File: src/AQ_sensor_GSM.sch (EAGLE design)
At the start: 82 parts, among them IC1 MIC29302WU, IC2 MCP73831/OT, J1 F-1X03-SIP-100-32, J2 SIM8060-6-1-14-00-A, Q1 MMBT2222, Q2 MMBT2222, Q3 MMBT2222, U2 TEXAS_INSTRUMENTS_SN74HC125TE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, U3 TEXAS_INSTRUMENTS_LM1117IMP-3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, U4 EC200UCNAB-N05-SNNSA, X1 53048-08

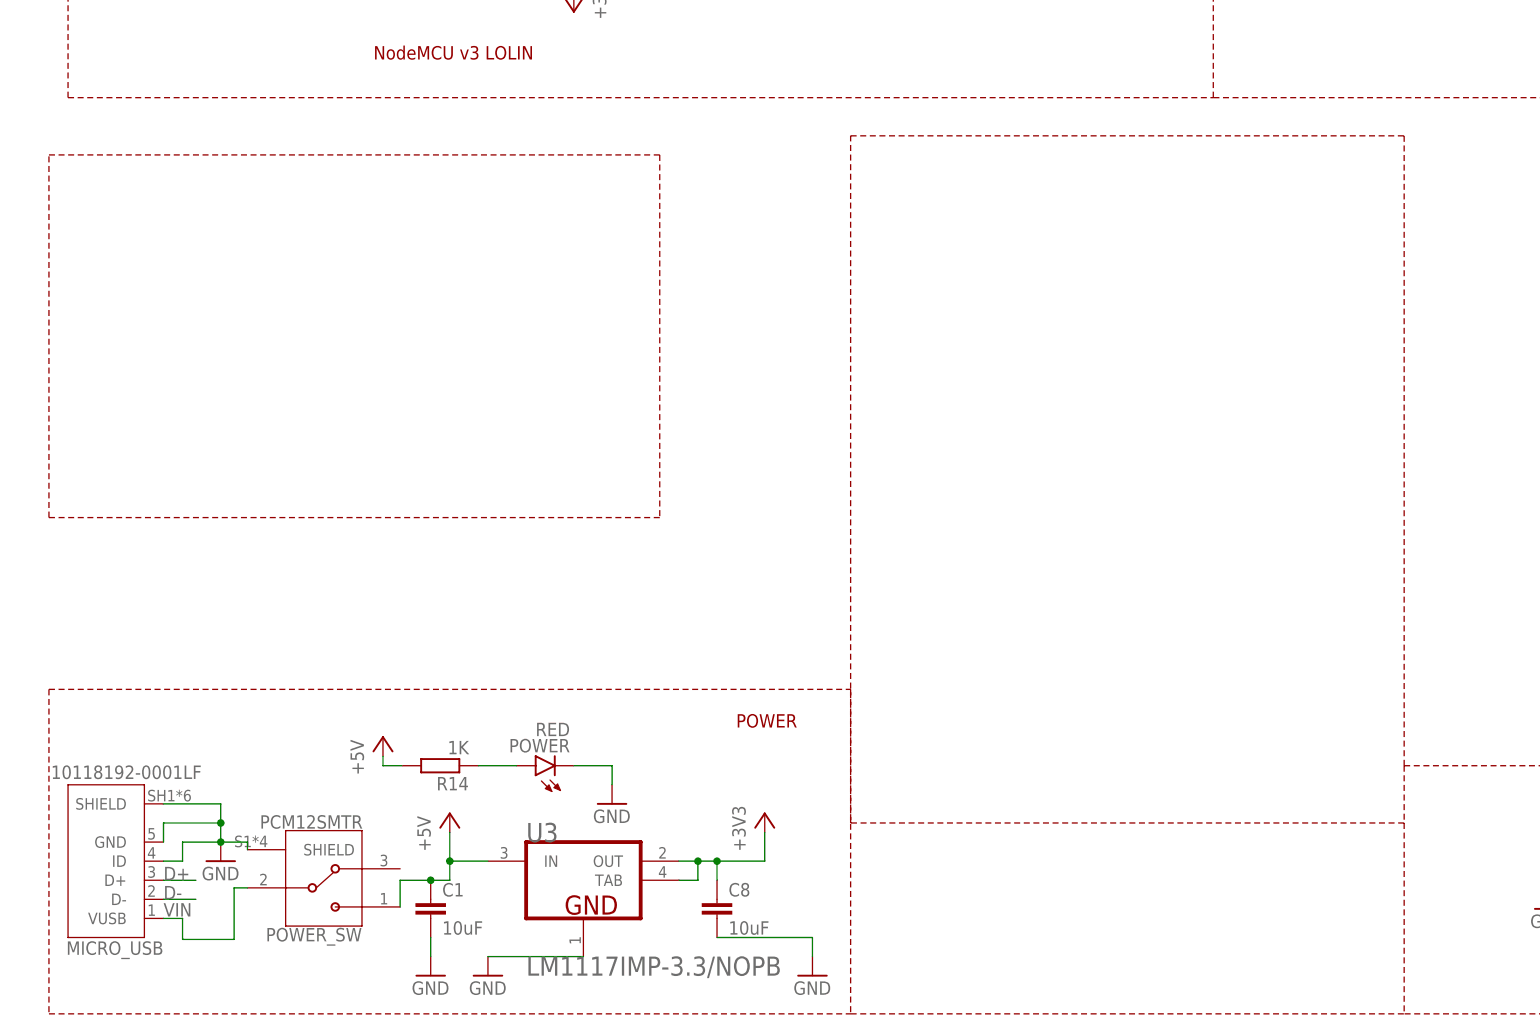
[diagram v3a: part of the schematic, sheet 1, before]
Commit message: Updated GSM antenna positions, pms connector, USB, and battery connector positions
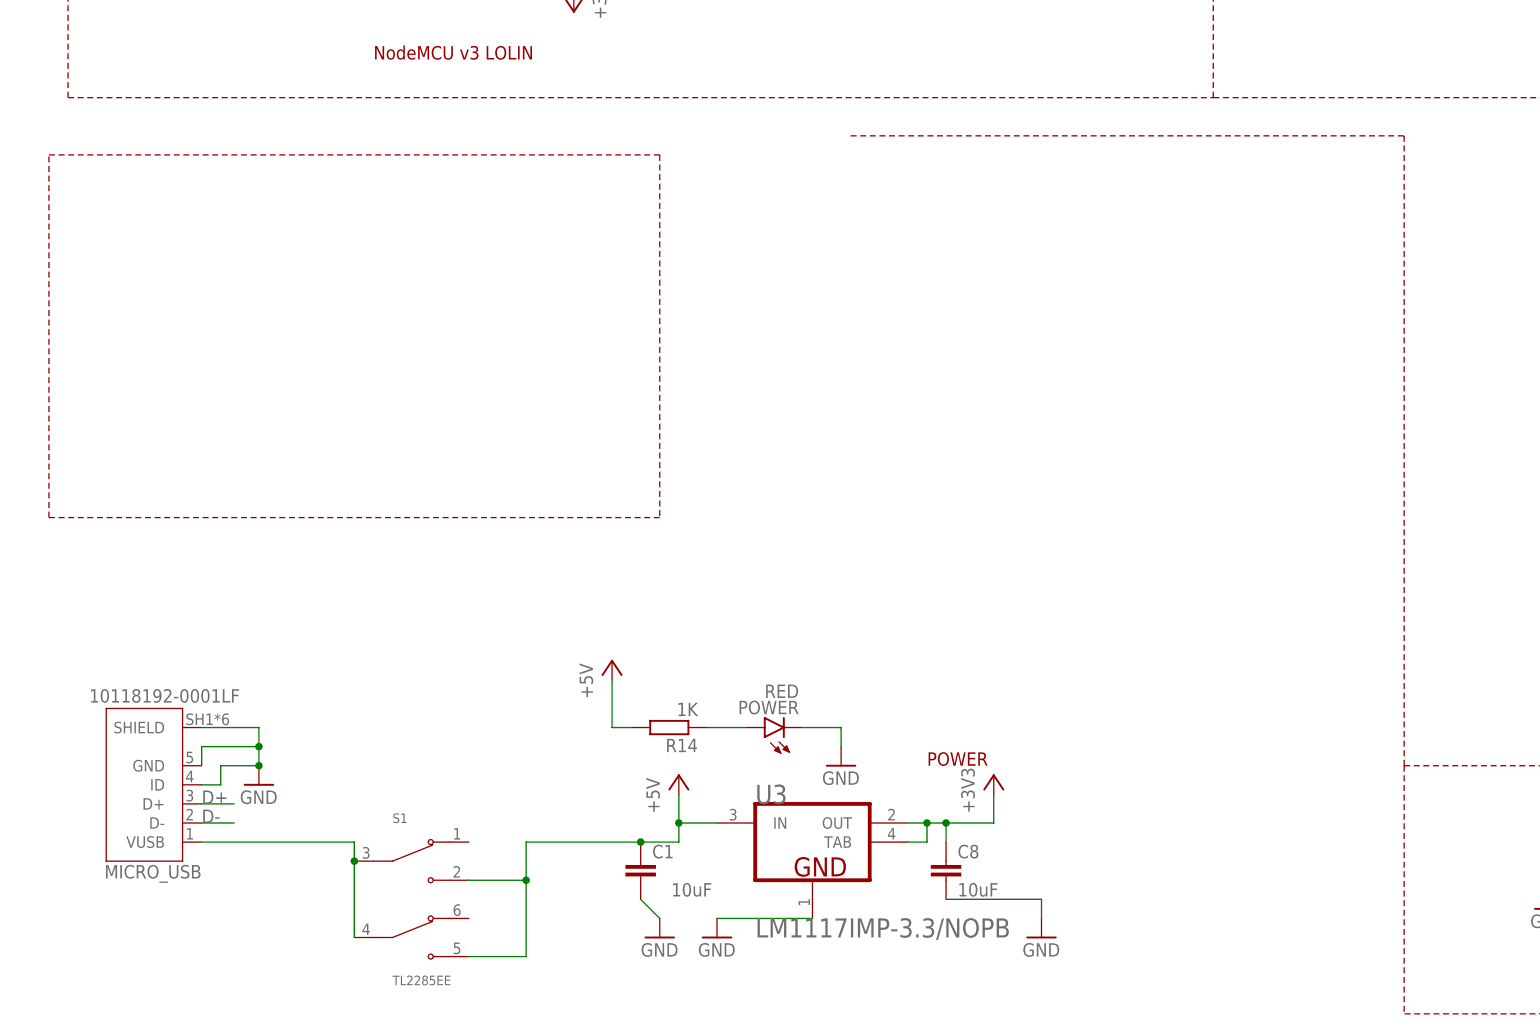
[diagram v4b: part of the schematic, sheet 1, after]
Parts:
- removed POWER_SW: PCM12SMTR, AQ_sensor_GSM:PCM12SMTR
- added S1: TL2285EE, TL2285EE:TL2285EE
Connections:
- removed net VIN: MICRO_USB.VUSB, POWER_SW.2
- new net N$17: MICRO_USB.VUSB, S1.COM1, S1.COM2
- net +5V: now also S1.NO1, S1.NO2; no longer POWER_SW.1
- net GND: no longer POWER_SW.SHIELD
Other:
- moved on the sheet: C1, C8, MICRO_USB, POWER, R14, U3

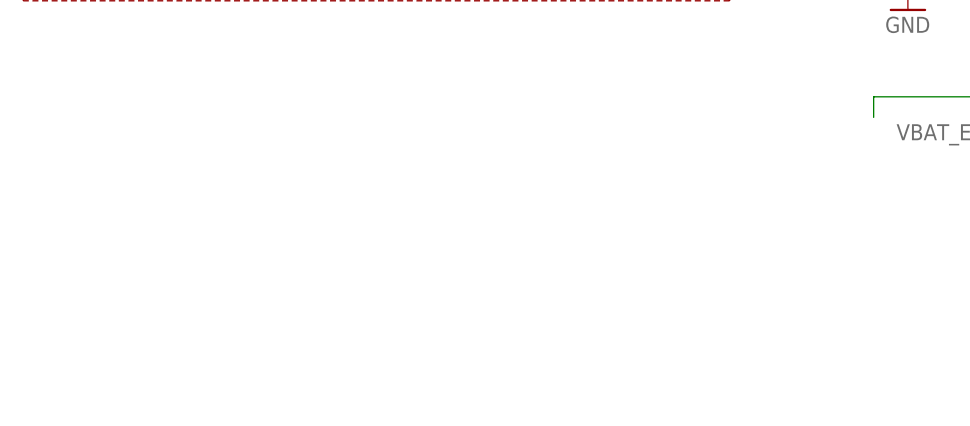
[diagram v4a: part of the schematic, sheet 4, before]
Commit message: Added dC jack
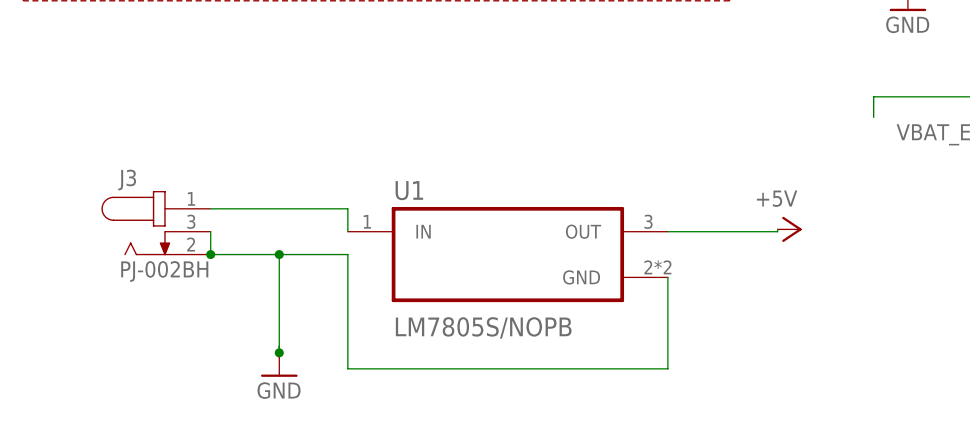
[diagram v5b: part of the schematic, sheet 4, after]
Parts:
- added J3: PJ-002BH, PJ-002BH:PJ-002BH
- added U1: LM7805S/NOPB, LM7805S_NOPB:LM7805S/NOPB
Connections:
- new net N$24: J3.1, U1.IN
- net +5V: now also U1.OUT
- net GND: now also J3.2, J3.3, U1.GND
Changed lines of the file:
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@@
 <part name="BT_ANT" library="SparkFun-Connectors" library_urn="urn:adsk.eagle:library:513" deviceset="CONN_01" device="" package3d_urn="urn:adsk.eagle:package:38028/1"/>
 <part name="S1" library="TL2285EE" deviceset="TL2285EE" device="" override_package3d_urn="urn:adsk.eagle:package:43003845/2" override_package_urn="urn:adsk.eagle:footprint:43003846/1"/>
+<part name="J3" library="PJ-002BH" deviceset="PJ-002BH" device="" override_package3d_urn="urn:adsk.eagle:package:43007122/2" override_package_urn="urn:adsk.eagle:footprint:43007123/1"/>
+<part name="U1" library="LM7805S_NOPB" deviceset="LM7805S/NOPB" device="" override_package3d_urn="urn:adsk.eagle:package:43007127/2" override_package_urn="urn:adsk.eagle:footprint:43007128/1"/>
+<part name="GND13" library="supply1" library_urn="urn:adsk.eagle:library:371" deviceset="GND" device=""/>
+<part name="P+10" library="supply1" library_urn="urn:adsk.eagle:library:371" deviceset="+5V" device=""/>
 </parts>
 <sheets>
@@
 <attribute name="VALUE" x="57.15" y="230.378" size="1.778" layer="96"/>
 </instance>
+<instance part="J3" gate="G$1" x="-88.9" y="144.78" smashed="yes">
+<attribute name="NAME" x="-93.98" y="149.86" size="1.778" layer="95"/>
+<attribute name="VALUE" x="-93.98" y="139.7" size="1.778" layer="96"/>
+</instance>
+<instance part="U1" gate="G$1" x="-50.8" y="142.24" smashed="yes">
+<attribute name="NAME" x="-63.5" y="148.32" size="2.0828" layer="95" ratio="10" rot="SR0"/>
+<attribute name="VALUE" x="-63.5" y="133.16" size="2.0828" layer="96" ratio="10" rot="SR0"/>
+</instance>
+<instance part="GND13" gate="1" x="-76.2" y="128.778" smashed="yes">
+<attribute name="VALUE" x="-78.74" y="126.238" size="1.778" layer="96"/>
+</instance>
+<instance part="P+10" gate="1" x="-18.288" y="145.034" smashed="yes" rot="R270">
+<attribute name="VALUE" x="-23.368" y="147.574" size="1.778" layer="96"/>
+</instance>
 </instances>
 <busses>
@@
 <wire x1="59.69" y1="235.458" x2="59.69" y2="246.38" width="0.1524" layer="91"/>
 <wire x1="59.69" y1="246.38" x2="60.96" y2="246.38" width="0.1524" layer="91"/>
+</segment>
+<segment>
+<pinref part="GND13" gate="1" pin="GND"/>
+<wire x1="-76.2" y1="132.08" x2="-76.2" y2="131.318" width="0.1524" layer="91"/>
+<pinref part="J3" gate="G$1" pin="3"/>
+<pinref part="J3" gate="G$1" pin="2"/>
+<wire x1="-83.82" y1="144.78" x2="-83.82" y2="142.24" width="0.1524" layer="91"/>
+<wire x1="-83.82" y1="142.24" x2="-76.2" y2="142.24" width="0.1524" layer="91"/>
+<wire x1="-76.2" y1="142.24" x2="-68.58" y2="142.24" width="0.1524" layer="91"/>
+<wire x1="-68.58" y1="142.24" x2="-68.58" y2="129.54" width="0.1524" layer="91"/>
+<junction x="-83.82" y="142.24"/>
+<pinref part="U1" gate="G$1" pin="GND"/>
+<wire x1="-68.58" y1="129.54" x2="-33.02" y2="129.54" width="0.1524" layer="91"/>
+<wire x1="-33.02" y1="129.54" x2="-33.02" y2="139.7" width="0.1524" layer="91"/>
+<wire x1="-76.2" y1="131.318" x2="-76.2" y2="142.24" width="0.1524" layer="91"/>
+<junction x="-76.2" y="131.318"/>
+<junction x="-76.2" y="142.24"/>
 </segment>
 </net>
@@
 <wire x1="-7.62" y1="187.96" x2="-7.62" y2="205.74" width="0.1524" layer="91"/>
 <wire x1="-7.62" y1="205.74" x2="58.42" y2="205.74" width="0.1524" layer="91"/>
+</segment>
+<segment>
+<pinref part="P+10" gate="1" pin="+5V"/>
+<pinref part="U1" gate="G$1" pin="OUT"/>
+<wire x1="-20.828" y1="145.034" x2="-20.828" y2="144.78" width="0.1524" layer="91"/>
+<wire x1="-20.828" y1="144.78" x2="-33.02" y2="144.78" width="0.1524" layer="91"/>
 </segment>
 </net>
@@
 </segment>
 </net>
+<net name="N$24" class="0">
+<segment>
+<pinref part="J3" gate="G$1" pin="1"/>
+<pinref part="U1" gate="G$1" pin="IN"/>
+<wire x1="-83.82" y1="147.32" x2="-68.58" y2="147.32" width="0.1524" layer="91"/>
+<wire x1="-68.58" y1="147.32" x2="-68.58" y2="144.78" width="0.1524" layer="91"/>
+</segment>
+</net>

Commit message: Rearrange USB port and DC jack
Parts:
- removed C14: EEEFT1E101AV, 100uf 25v capacitor:EEEFT1E101AV
- removed C5: EEEFN1C471P, EEEFN1C471P:EEEFN1C471P
- removed D4: ON_SEMI_1N4148WSON_SEMI_1N4148WS_0_0, AQ_sensor_GSM:ON_SEMI_1N4148WSON_SEMI_1N4148WS_0_0
- removed NET: YELLOW, led:LEDCHIP-LED0603
- removed PWR: RED, led:LEDCHIP-LED0603
- removed R1, R6, R7: 470, rcl:R-EU_R0603
- removed RI: ORANGE, led:LEDCHIP-LED0603
- removed U2: TEXAS_INSTRUMENTS_SN74HC125TEXAS_INSTRUMENTS_SN74HC125_0_0, AQ_sensor_GSM:TEXAS_INSTRUMENTS_SN74HC125TEXAS_INSTRUMENTS_SN74HC125_0_0
- added C19, C20: 100nf, 06035C104K4T2A:06035C104K4T2A
- added LIPO_SW: TL2285EE, TL2285EE:TL2285EE
- added M_RI, N_MODE, N_STAT, P_STAT: ORANGE, led:LEDCHIP-LED0603
- added Q4, Q5, Q6, Q7: MMBT2222, MMBT2222_:MMBT2222
- added R23, R31, R34: 4.7K, rcl:R-EU_R0603
- added R24, R32, R35: 47K, rcl:R-EU_R0603
- added R25, R28, R33, R36: 470R, rcl:R-EU_R0603
- added R26: 120K, rcl:R-EU_R0603
- added R27: 10K, rcl:R-EU_R0603
- added R29, R30: 51K, rcl:R-EU_R0603
- added U5: TXS0108EPWR, TXS0108EPWR:TXS0108EPWR
- R12: value 0R -> 4.7K; device CR0805AJ_-000EAS:CR0805AJ/-000EAS -> rcl:R-EU_R0603
- R13: value 100M -> 47K; device CR0805AJ_-000EAS:CR0805AJ/-000EAS -> rcl:R-EU_R0603
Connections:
- removed net GSM_RX: D4.ANODE, U4.MAIN_RXD
- removed net GSM_RX_O: D4.CATHODE, SV1.8
- removed net GSM_TX: U2B.2A, U4.MAIN_TXD
- removed net GSM_TX_5V: SV1.7, U2B.2Y
- removed net N$10: NET.A, R6.2
- removed net N$11: PWR.A, R7.2
- removed net N$14: R1.2, RI.A
- removed net NETSTAT_5V: R6.1, U2A.1Y
- removed net PWRSTAT_5V: R7.1, U2C.3Y
- removed net RI: U2D.4A, U4.MAIN_RI
- removed net RI_5V: RI.C, U2D.4Y
- new net BP: CN1.2, IC2.VBAT, LIPO_SW.NC1, LIPO_SW.NC2
- new net CP: C6.1, C7.2, D5.K, IC1.OUT, LIPO_SW.NO1, LIPO_SW.NO2, R11.2, R9.2
- new net MAIN_CTS: U4.MAIN_CTS, U5.A3
- new net MAIN_DCD: U4.MAIN_DCD, U5.A2
- new net MAIN_DTR: U4.MAIN_DTR, U5.A5
- new net MAIN_RI: R34.1, U4.MAIN_RI, U5.A1
- new net MAIN_RTS: U4.MAIN_RTS, U5.A4
- new net MAIN_RXD: U4.MAIN_RXD, U5.A7
- new net MAIN_TXD: U4.MAIN_TXD, U5.A6
- new net MCU_CTS: U5.B3
- new net MCU_DCD: U5.B2
- new net MCU_DTR: SV2.12, U5.B5
- new net MCU_RI: U5.B1
- new net MCU_RTS: U5.B4
- new net MCU_RXD: SV1.8, U5.B6
- new net MCU_TXD: SV1.7, U5.B7
- new net N$26: Q4.B, R23.2, R24.2
- new net N$28: Q6.B, R31.2, R32.2
- new net N$29: Q4.C, R25.1
- new net N$30: N_MODE.C, R25.2
- new net N$31: R26.1, R27.2, U5.OE
- new net N$32: Q6.C, R33.1
- new net N$40: R30.1, U5.A8
- new net N$41: R29.1, U5.B8
- new net N$42: Q7.B, R34.2, R35.2
- new net N$43: Q7.C, R36.1
- new net N$44: M_RI.C, R36.2
- new net NET_MODE: R23.1, U4.NET_MODE
- net +3V3: now also C20.2, U5.VCCB
- net +5V: no longer C5.1, R1.1, U2E.VCC
- net GND: now also C19.1, C20.1, Q4.E, Q5.E, Q6.E, Q7.E, R13.1, R24.1, R26.2, R29.2, R30.2, R32.1, R35.1, U5.GND; no longer C14.2, C5.2, NET.C, PWR.C, U2A.1_!OE!, U2B.4_!OE!, U2C.2_!OE!, U2D.3_!OE!, U2E.GND
- net N$22: now also Q5.B, R12.2, R13.2; no longer SV2.12
- net N$33: now also Q5.C, R28.1; no longer U4.MAIN_DTR
- net N$34: now also N_STAT.C, R28.2; no longer C6.1, C7.2, D5.K, IC1.OUT, R11.2, R13.1, R9.2
- net N$39: now also P_STAT.C, R33.2; no longer CN1.2, IC2.VBAT, R12.2
- net NETSTAT: now also R12.1; no longer U2A.1A
- net PWRSTAT: now also R31.1; no longer U2C.3A
- net VDD_EXT: now also C19.2, R27.1, U5.VCCA
- net V_LIPO: now also LIPO_SW.COM1, LIPO_SW.COM2, M_RI.A, N_MODE.A, N_STAT.A, P_STAT.A; no longer C14.1, R12.1, R13.2
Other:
- note removed: "LEVEL SHIFTER"
- note removed: "STATUS LEDS"

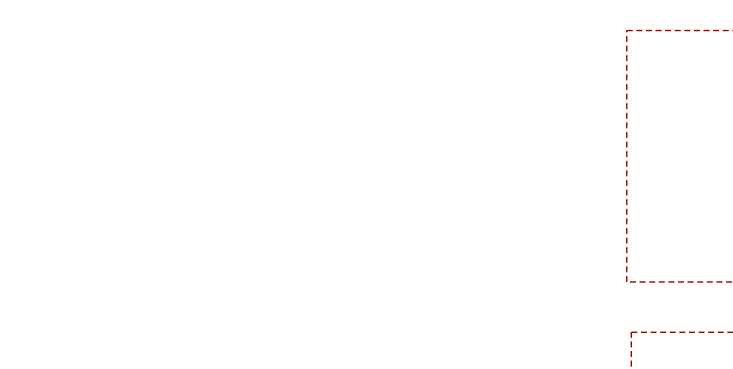
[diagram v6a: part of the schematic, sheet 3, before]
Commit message: Added internal gsm Antenna
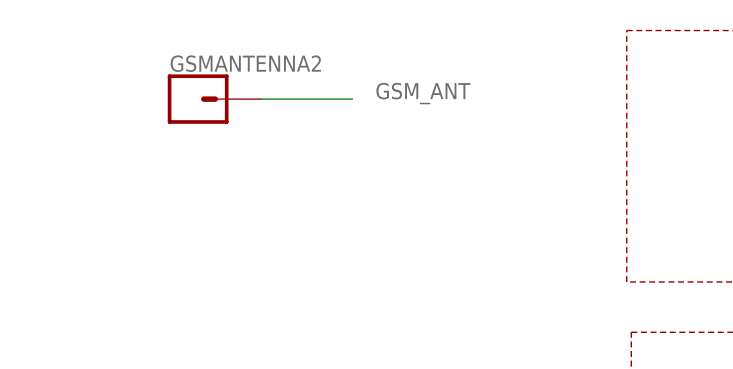
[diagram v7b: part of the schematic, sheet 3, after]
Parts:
- added GSMANTENNA2: (no value), SparkFun-Connectors:CONN_01
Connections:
- net GSM_ANT: now also GSMANTENNA2.1
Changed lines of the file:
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@@
 <part name="M_RI" library="led" library_urn="urn:adsk.eagle:library:259" deviceset="LED" device="CHIP-LED0603" package3d_urn="urn:adsk.eagle:package:15819/3" value="ORANGE"/>
 <part name="C2" library="T495X477K010ATE100" deviceset="T495X477K010ATE100" device="" override_package3d_urn="urn:adsk.eagle:package:43000626/2" override_package_urn="urn:adsk.eagle:footprint:43000628/1" value="470uf"/>
+<part name="GSMANTENNA2" library="SparkFun-Connectors" library_urn="urn:adsk.eagle:library:513" deviceset="CONN_01" device="" package3d_urn="urn:adsk.eagle:package:38028/1"/>
 </parts>
 <sheets>
@@
 <attribute name="NAME" x="-180.34" y="198.628" size="1.778" layer="95" font="vector"/>
 </instance>
+<instance part="GSMANTENNA2" gate="G$1" x="-182.88" y="241.3" smashed="yes">
+<attribute name="VALUE" x="-185.42" y="236.474" size="1.778" layer="96" font="vector"/>
+<attribute name="NAME" x="-185.42" y="244.348" size="1.778" layer="95" font="vector"/>
+</instance>
 </instances>
 <busses>
@@
 <label x="-30.48" y="205.74" size="1.778" layer="95"/>
 </segment>
-</net>
+<segment>
+<pinref part="GSMANTENNA2" gate="G$1" pin="1"/>
+<wire x1="-175.26" y1="241.3" x2="-165.1" y2="241.3" width="0.1524" layer="91"/>
+<label x="-162.56" y="241.3" size="1.778" layer="95"/>
+</segment>
+</net>

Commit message: Routed
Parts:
- removed CN1: (no value), AQ_sensor_GSM:JST_2PIN-SMT-RA
- removed GPS, GSM: 50 Ohms, AQ_sensor_GSM:SMACONNECTOR_EDGE_UFL
- removed TP1, TP2: TPB1,27, testpad:TPB1,27
- added J4: 78646-3001, 78646-3001:78646-3001
- added J5: 20579-001E, 20579-001E:20579-001E
- added J6: 2828XX-2282837-2, Connector:2828XX-2282837-2
- J2: value SIM8060-6-1-14-00-A -> 20579-001E; device Sim card nano XKNANO:SIM8060-6-1-14-00-A -> 20579-001E:20579-001E
- renumbered S1 to PSW
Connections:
- net N$17 renamed VUSB
- removed net 1.8V: TP1.TP
- removed net 2.8V: TP2.TP
- removed net BP: CN1.2, IC2.VBAT, LIPO_SW.NC1, LIPO_SW.NC2
- removed net N$3: J2.VPP
- new net BATT-PW: IC2.VBAT, J6.2, LIPO_SW.NC1, LIPO_SW.NC2
- new net N$11: J4.VPP
- net GND: now also J2.GROUND, J5.GROUND, J6.1; no longer CN1.1, GPS.GND1, GPS.GND2, GPS.GND3, GPS.GND4, GSM.GND1, GSM.GND2, GSM.GND3, GSM.GND4, J2.SHIELD
- net GNSS_ANT: now also J5.SIGNAL; no longer GPS.ANT
- net GSM_ANT: now also J2.SIGNAL; no longer GSM.ANT
- net SIMCLK: now also J4.CLK; no longer J2.CLK
- net SIMDATA: now also J4.I/O; no longer J2.IO
- net SIMRST: now also J4.RST; no longer J2.RST
- net USIM_DET: no longer J2.SW
- net USIM_GND: now also J4.GND; no longer J2.GND
- net USIM_VDD: now also J4.VCC; no longer J2.VCC
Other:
- note removed: "TEST PADS"
- moved on the sheet: BT_ANT, GSMANTENNA2
